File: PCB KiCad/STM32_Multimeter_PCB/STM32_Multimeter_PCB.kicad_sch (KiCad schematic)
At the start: 57 parts, among them J1 Conn_01x02_Pin, J2 USB_B_Micro, J3 Conn_01x04_Pin, J4 Conn_Coaxial, J5 Conn_01x03_Pin, SW1 SW_Push, SW3 SW_Push, SW4 SW_DPDT_x2, U1 STM32WB55CGUx, U10 AMS1117-3.3, U11 4051, U3 LTC4054XES5-4.2, U3 TPS61040DBV, U4 DW01A, U5 FS8205A, Y1 Crystal 32 MHz

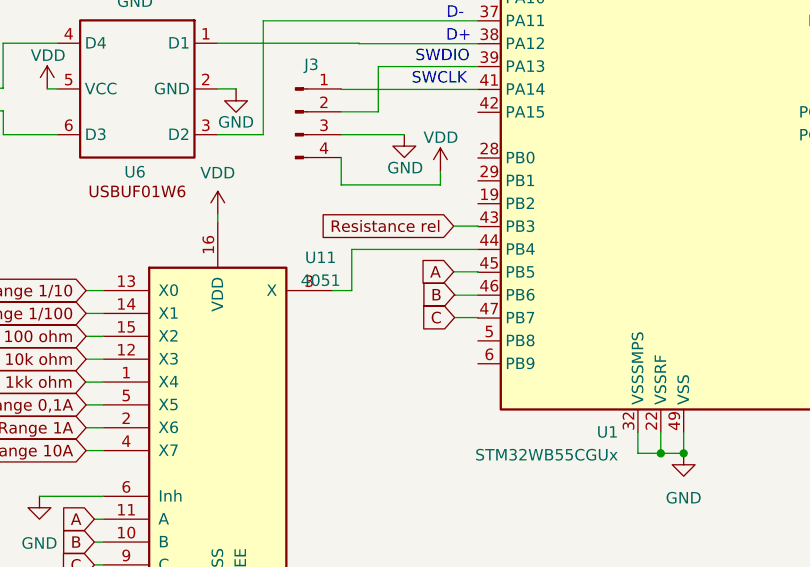
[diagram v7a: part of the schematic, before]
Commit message: Created pcb schematic
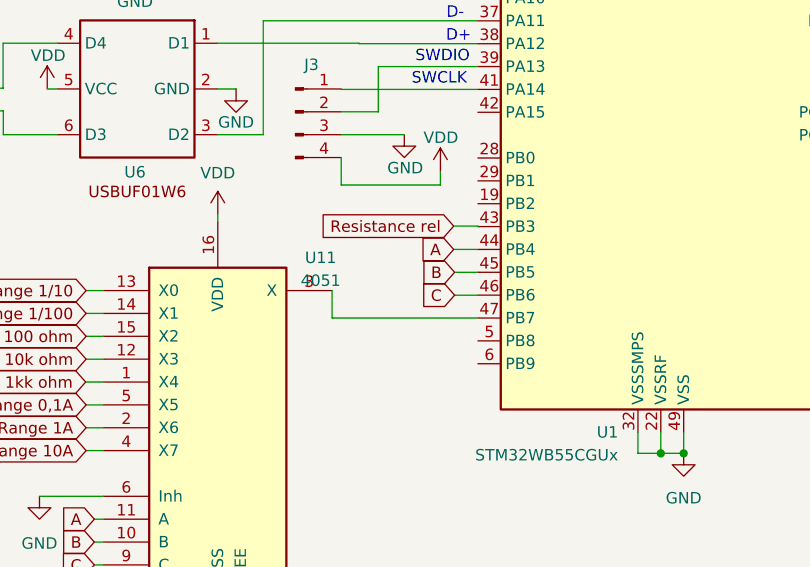
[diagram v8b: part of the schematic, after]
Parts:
- D2: footprint Diode_SMD:D_SMA_Handsoldering -> Diode_SMD:D_SMA
- L1, L2, L4: footprint Inductor_SMD:L_Taiyo-Yuden_NR-50xx -> Inductor_SMD:L_0805_2012Metric
- SW1, SW3: footprint (none) -> Button_Switch_SMD:SW_SPST_FSMSM
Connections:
- net A: now also U1.44 (PB4); no longer U1.45 (PB5)
- net B: now also U1.45 (PB5); no longer U1.46 (PB6)
- net C: now also U1.46 (PB6); no longer U1.47 (PB7)
- net at U11.3 (X): now also U1.47 (PB7); no longer U1.44 (PB4)
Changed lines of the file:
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@@
     (stroke (width 0) (type default))
   )
+  (wire (pts (xy 69.6468 154.5844) (xy 85.852 154.5844))
+    (stroke (width 0) (type default))
+  )
   (wire (pts (xy 134.5184 35.2552) (xy 134.5184 35.6616))
     (stroke (width 0) (type default))
@@
     (stroke (width 0) (type default))
   )
-  (wire (pts (xy 85.852 152.0444) (xy 83.2612 152.0444))
-    (stroke (width 0) (type default))
-  )
   (wire (pts (xy 63.8048 73.66) (xy 63.8048 73.6092))
     (stroke (width 0) (type default))
@@
     (stroke (width 0) (type default))
   )
-  (wire (pts (xy 85.852 154.5336) (xy 85.852 154.5844))
-    (stroke (width 0) (type default))
-  )
-  (wire (pts (xy 71.8312 151.5364) (xy 69.6468 151.5364))
-    (stroke (width 0) (type default))
-  )
   (wire (pts (xy 69.4944 32.9692) (xy 69.4944 32.3342))
     (stroke (width 0) (type default))
   )
-  (wire (pts (xy 83.1596 149.4536) (xy 85.852 149.4536))
-    (stroke (width 0) (type default))
-  )
   (wire (pts (xy 237.2868 36.83) (xy 237.2868 36.8203))
     (stroke (width 0) (type default))
@@
     (stroke (width 0) (type default))
   )
-  (wire (pts (xy 85.852 149.4536) (xy 85.852 149.5044))
-    (stroke (width 0) (type default))
-  )
   (wire (pts (xy 254.254 80.8736) (xy 255.5678 80.8736))
     (stroke (width 0) (type default))
@@
     (stroke (width 0) (type default))
   )
+  (wire (pts (xy 83.2612 152.0444) (xy 85.852 152.0444))
+    (stroke (width 0) (type default))
+  )
   (wire (pts (xy 33.1216 134.2136) (xy 39.116 134.2136))
     (stroke (width 0) (type default))
@@
     (stroke (width 0) (type default))
   )
+  (wire (pts (xy 83.2612 149.5044) (xy 85.852 149.5044))
+    (stroke (width 0) (type default))
+  )
   (wire (pts (xy 237.8456 52.2224) (xy 238.4552 52.2224))
     (stroke (width 0) (type default))
@@
     (stroke (width 0) (type default))
   )
-  (wire (pts (xy 85.852 146.9644) (xy 71.8312 146.9644))
-    (stroke (width 0) (type default))
-  )
   (wire (pts (xy 82.8548 93.6244) (xy 82.8548 93.6752))
     (stroke (width 0) (type default))
@@
     (stroke (width 0) (type default))
   )
+  (wire (pts (xy 69.6468 151.5364) (xy 69.6468 154.5844))
+    (stroke (width 0) (type default))
+  )
   (wire (pts (xy 63.8048 73.6092) (xy 50.5968 73.6092))
     (stroke (width 0) (type default))
@@
     (stroke (width 0) (type default))
   )
-  (wire (pts (xy 71.8312 146.9644) (xy 71.8312 151.5364))
-    (stroke (width 0) (type default))
-  )
   (wire (pts (xy 69.5769 49.4792) (xy 69.5769 45.1866))
     (stroke (width 0) (type default))
@@
     (stroke (width 0) (type default))
   )
-  (wire (pts (xy 83.2612 154.5336) (xy 85.852 154.5336))
-    (stroke (width 0) (type default))
-  )
   (wire (pts (xy 44.2468 161.6964) (xy 42.2656 161.6964))
     (stroke (width 0) (type default))
@@
     (stroke (width 0) (type default))
   )
-  (wire (pts (xy 83.2612 152.0444) (xy 83.2612 151.9936))
-    (stroke (width 0) (type default))
-  )
   (wire (pts (xy 197.4596 120.8532) (xy 197.4596 120.904))
     (stroke (width 0) (type default))
@@
     (stroke (width 0) (type default))
   )
+  (wire (pts (xy 83.1596 146.9644) (xy 85.852 146.9644))
+    (stroke (width 0) (type default))
+  )
   (wire (pts (xy 218.8464 120.9548) (xy 209.2452 120.9548))
     (stroke (width 0) (type default))
@@
     )
   )
-  (global_label "B" (shape input) (at 83.2612 151.9936 180) (fields_autoplaced)
+  (global_label "B" (shape input) (at 83.2612 149.5044 180) (fields_autoplaced)
     (effects (font (size 1.27 1.27)) (justify right))
-    (property "Intersheetrefs" "${INTERSHEET_REFS}" (at 79.006 151.9936 0)
+    (property "Intersheetrefs" "${INTERSHEET_REFS}" (at 79.006 149.5044 0)
       (effects (font (size 1.27 1.27)) (justify right) hide)
     )
@@
     )
   )
-  (global_label "A" (shape input) (at 83.1596 149.4536 180) (fields_autoplaced)
+  (global_label "A" (shape input) (at 83.1596 146.9644 180) (fields_autoplaced)
     (effects (font (size 1.27 1.27)) (justify right))
-    (property "Intersheetrefs" "${INTERSHEET_REFS}" (at 79.0858 149.4536 0)
+    (property "Intersheetrefs" "${INTERSHEET_REFS}" (at 79.0858 146.9644 0)
       (effects (font (size 1.27 1.27)) (justify right) hide)
     )
@@
     )
   )
-  (global_label "C" (shape input) (at 83.2612 154.5336 180) (fields_autoplaced)
+  (global_label "C" (shape input) (at 83.2612 152.0444 180) (fields_autoplaced)
     (effects (font (size 1.27 1.27)) (justify right))
-    (property "Intersheetrefs" "${INTERSHEET_REFS}" (at 79.006 154.5336 0)
+    (property "Intersheetrefs" "${INTERSHEET_REFS}" (at 79.006 152.0444 0)
       (effects (font (size 1.27 1.27)) (justify right) hide)
     )
@@
       (effects (font (size 1.27 1.27)))
     )
-    (property "Footprint" "Diode_SMD:D_SMA_Handsoldering" (at 61.8744 20.2692 0)
+    (property "Footprint" "Diode_SMD:D_SMA" (at 61.8744 20.2692 0)
       (effects (font (size 1.27 1.27)) hide)
     )
@@
       (effects (font (size 1.27 1.27)))
     )
-    (property "Footprint" "" (at 172.8724 73.1012 0)
+    (property "Footprint" "Button_Switch_SMD:SW_SPST_FSMSM" (at 172.8724 73.1012 0)
       (effects (font (size 1.27 1.27)) hide)
     )
@@
       (effects (font (size 1.27 1.27)))
     )
-    (property "Footprint" "Inductor_SMD:L_Taiyo-Yuden_NR-50xx" (at 132.5372 73.8632 0)
+    (property "Footprint" "Inductor_SMD:L_0805_2012Metric" (at 132.5372 73.8632 0)
       (effects (font (size 1.27 1.27)) hide)
     )
@@
       (effects (font (size 1.27 1.27)))
     )
-    (property "Footprint" "Inductor_SMD:L_Taiyo-Yuden_NR-50xx" (at 201.2696 120.904 0)
+    (property "Footprint" "Inductor_SMD:L_0805_2012Metric" (at 201.2696 120.904 0)
       (effects (font (size 1.27 1.27)) hide)
     )
@@
       (effects (font (size 1.27 1.27)))
     )
-    (property "Footprint" "Inductor_SMD:L_Taiyo-Yuden_NR-50xx" (at 151.9428 98.7044 0)
+    (property "Footprint" "Inductor_SMD:L_0805_2012Metric" (at 151.9428 98.7044 0)
       (effects (font (size 1.27 1.27)) hide)
     )
@@
       (effects (font (size 1.27 1.27)))
     )
-    (property "Footprint" "" (at 165.2524 144.018 0)
+    (property "Footprint" "Button_Switch_SMD:SW_SPST_FSMSM" (at 165.2524 144.018 0)
       (effects (font (size 1.27 1.27)) hide)
     )
